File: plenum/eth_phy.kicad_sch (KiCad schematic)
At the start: 4 parts

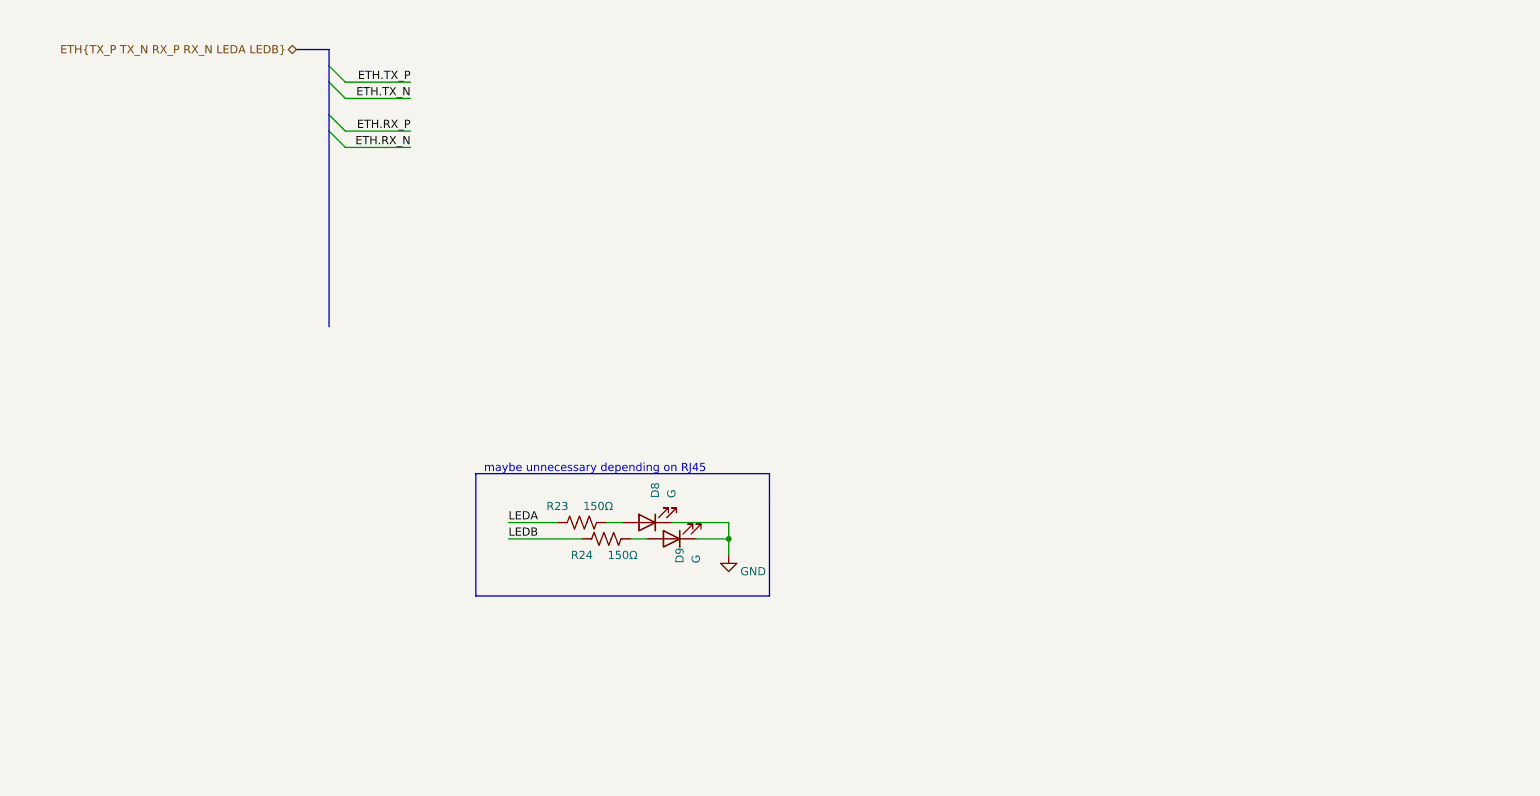
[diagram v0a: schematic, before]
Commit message: adding notes and BMI270 IMU to plenum
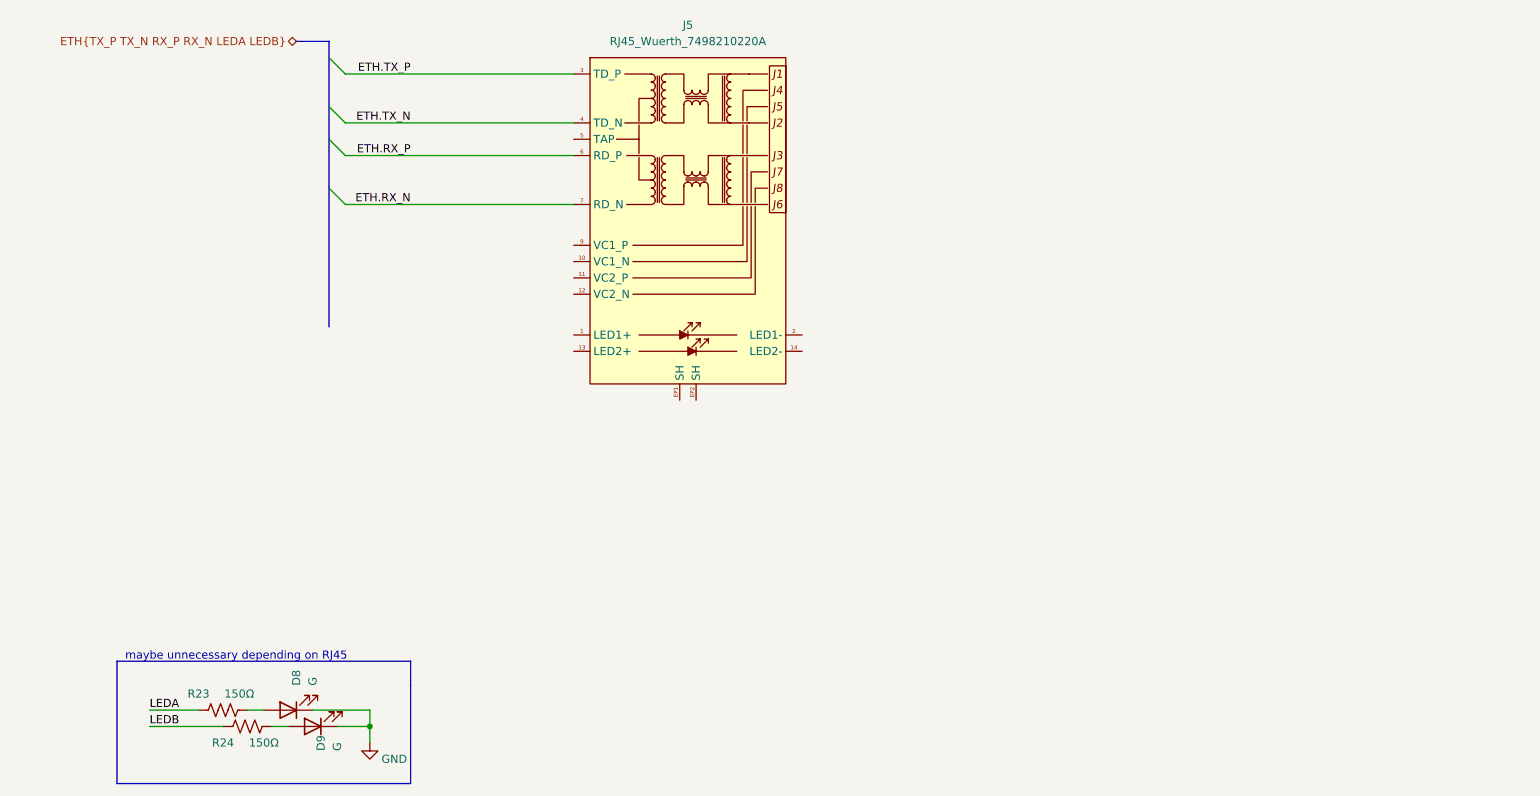
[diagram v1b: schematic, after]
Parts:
- added J5: RJ45_Wuerth_7498210220A, Connector_RJ:RJ45_Wuerth_7498210220A_Horizontal, symbol Connector:RJ45_Wuerth_7498210220A
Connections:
- net ETH.RX_N: now also J5.7 (RD_N)
- net ETH.RX_P: now also J5.6 (RD_P)
- net ETH.TX_N: now also J5.4 (TD_N)
- net ETH.TX_P: now also J5.3 (TD_P)
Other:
- moved on the sheet: D8, D9, R23, R24

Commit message: adding housekeeping board
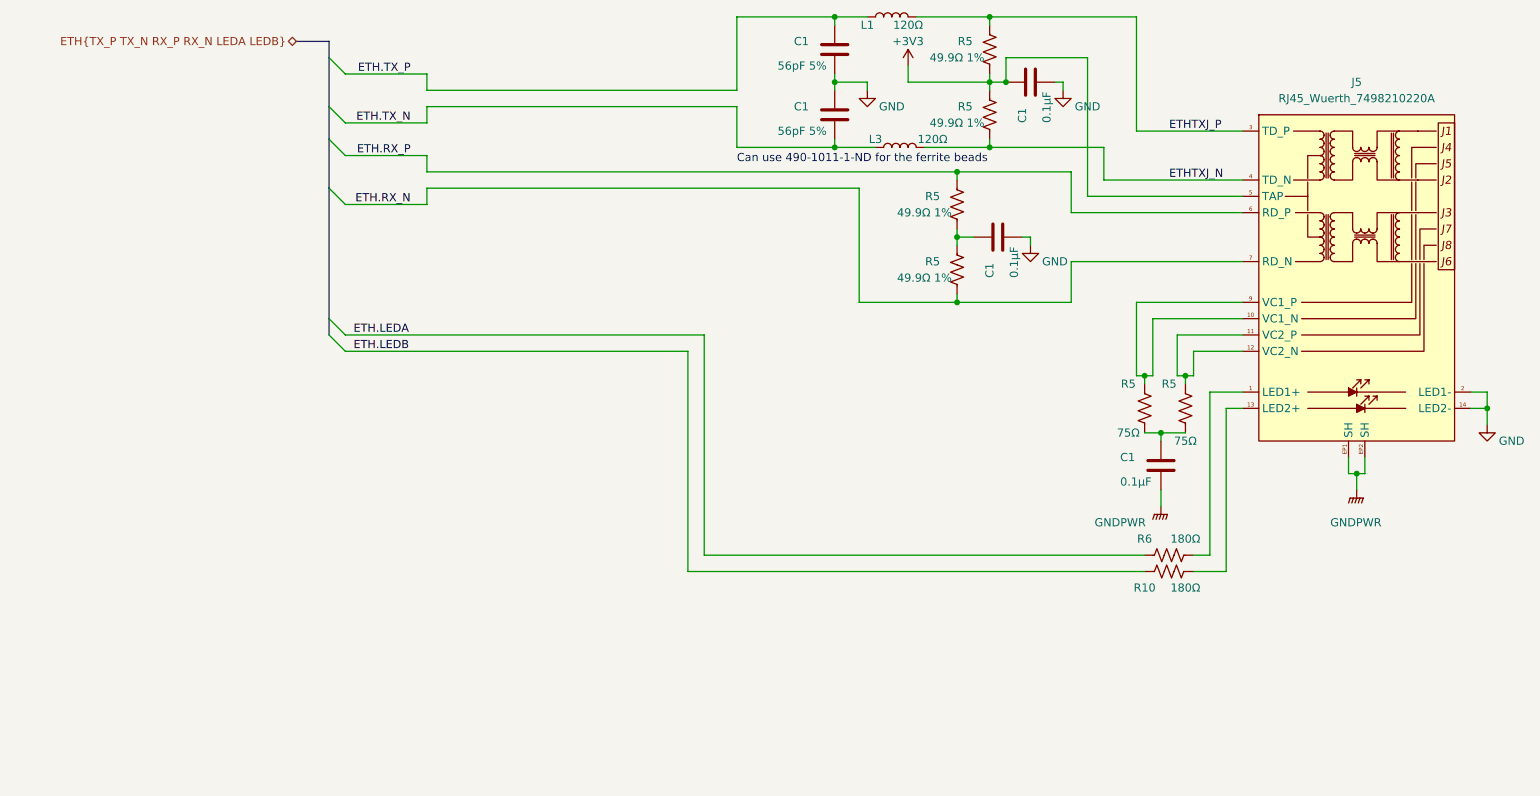
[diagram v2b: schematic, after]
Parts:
- removed D8, D9: G, symbol Device:LED
- removed R23, R24: 150Ω, Resistor_SMD:R_0603_1608Metric, symbol Device:R_US
- added C1 (x2): 56pF 5%, Capacitor_SMD:C_0603_1608Metric, symbol Device:C
- added C1 (x3): 0.1µF, Capacitor_SMD:C_1206_3216Metric, symbol Device:C
- added L1, L3: 120Ω, Resistor_SMD:R_0603_1608Metric, symbol Device:L
- added R10, R6: 180Ω, Resistor_SMD:R_0603_1608Metric, symbol Device:R_US
- added R5 (x4): 49.9Ω 1%, Resistor_SMD:R_0603_1608Metric, symbol Device:R_US
- added R5 (x2): 75Ω, Resistor_SMD:R_0603_1608Metric, symbol Device:R_US
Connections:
- net ETH.RX_N: now also R5.1
- net ETH.RX_P: now also R5.2
- net ETH.TX_N: now also C1.2, L3.1; no longer J5.4 (TD_N)
- net ETH.TX_P: now also C1.1, L1.1; no longer J5.3 (TD_P)
- net GND: now also J5.14 (LED2-), J5.2 (LED1-), C1.1, C1.2, C1.2, C1.2
- net at J5.1 (LED1+): now also R6.1
- net at J5.10 (VC1_N): now also J5.9 (VC1_P), R5.2
- net at J5.11 (VC2_P): now also J5.12 (VC2_N), R5.2
- net at J5.13 (LED2+): now also R10.1
- net +3V3: now reaches J5.5 (TAP)
- net +3V3: now also C1.1, R5.1, R5.2
- net GNDPWR: now reaches J5.EP1 (SH)
- net GNDPWR: now also J5.EP2 (SH), C1.2
- new net: C1.1, R5.1, R5.2
- new net: C1.1, R5.1, R5.1
- new net ETH.LEDA: R6.2
- new net ETH.LEDB: R10.2
- new net ETHTXJ_N: J5.4 (TD_N), L3.2, R5.1
- new net ETHTXJ_P: J5.3 (TD_P), L1.2, R5.2
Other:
- note added: "Can use 490-1011-1-ND for the ferrite beads"
- note removed: "maybe unnecessary depending on RJ45"
- moved on the sheet: J5
